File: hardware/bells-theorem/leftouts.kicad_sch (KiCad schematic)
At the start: 51 parts, among them U10 TLV9304, U8 TLV9304, U9 TLV9304

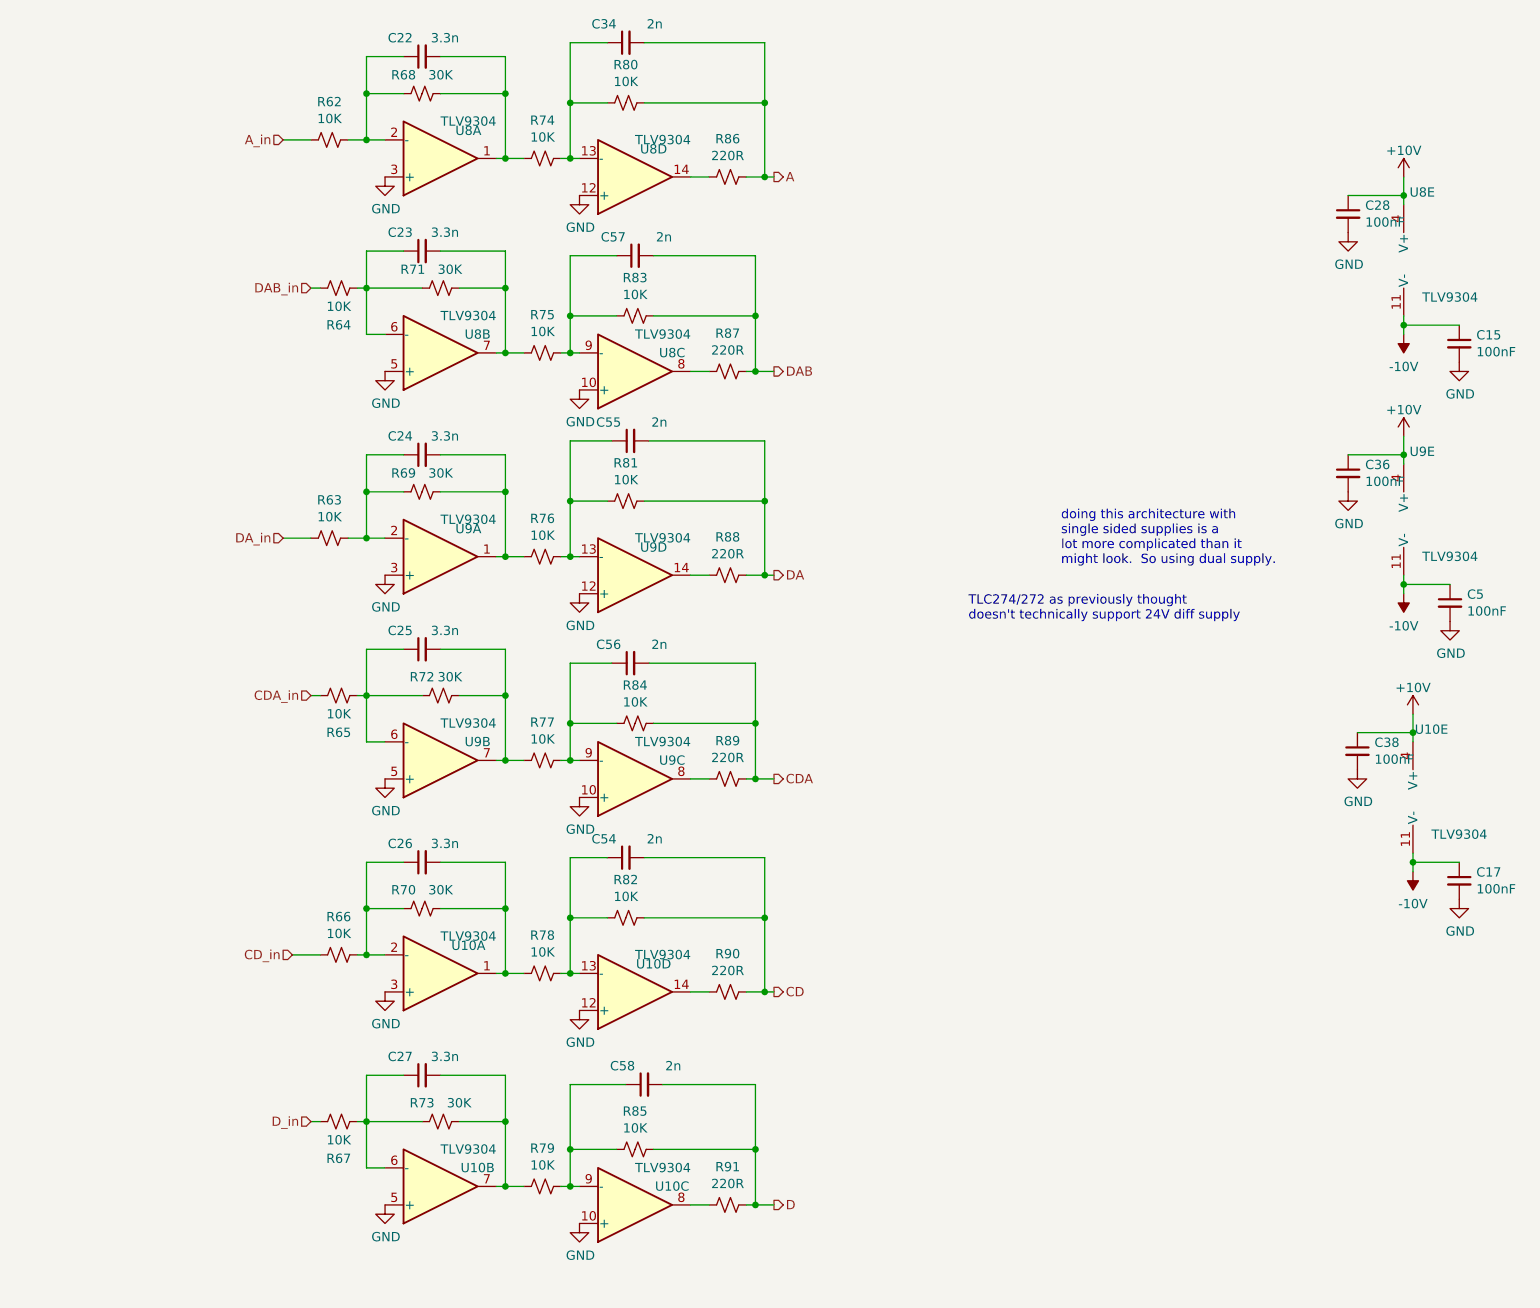
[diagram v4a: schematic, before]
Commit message: current revision actually 0.6 was 1.0 candidate, but needs major revision
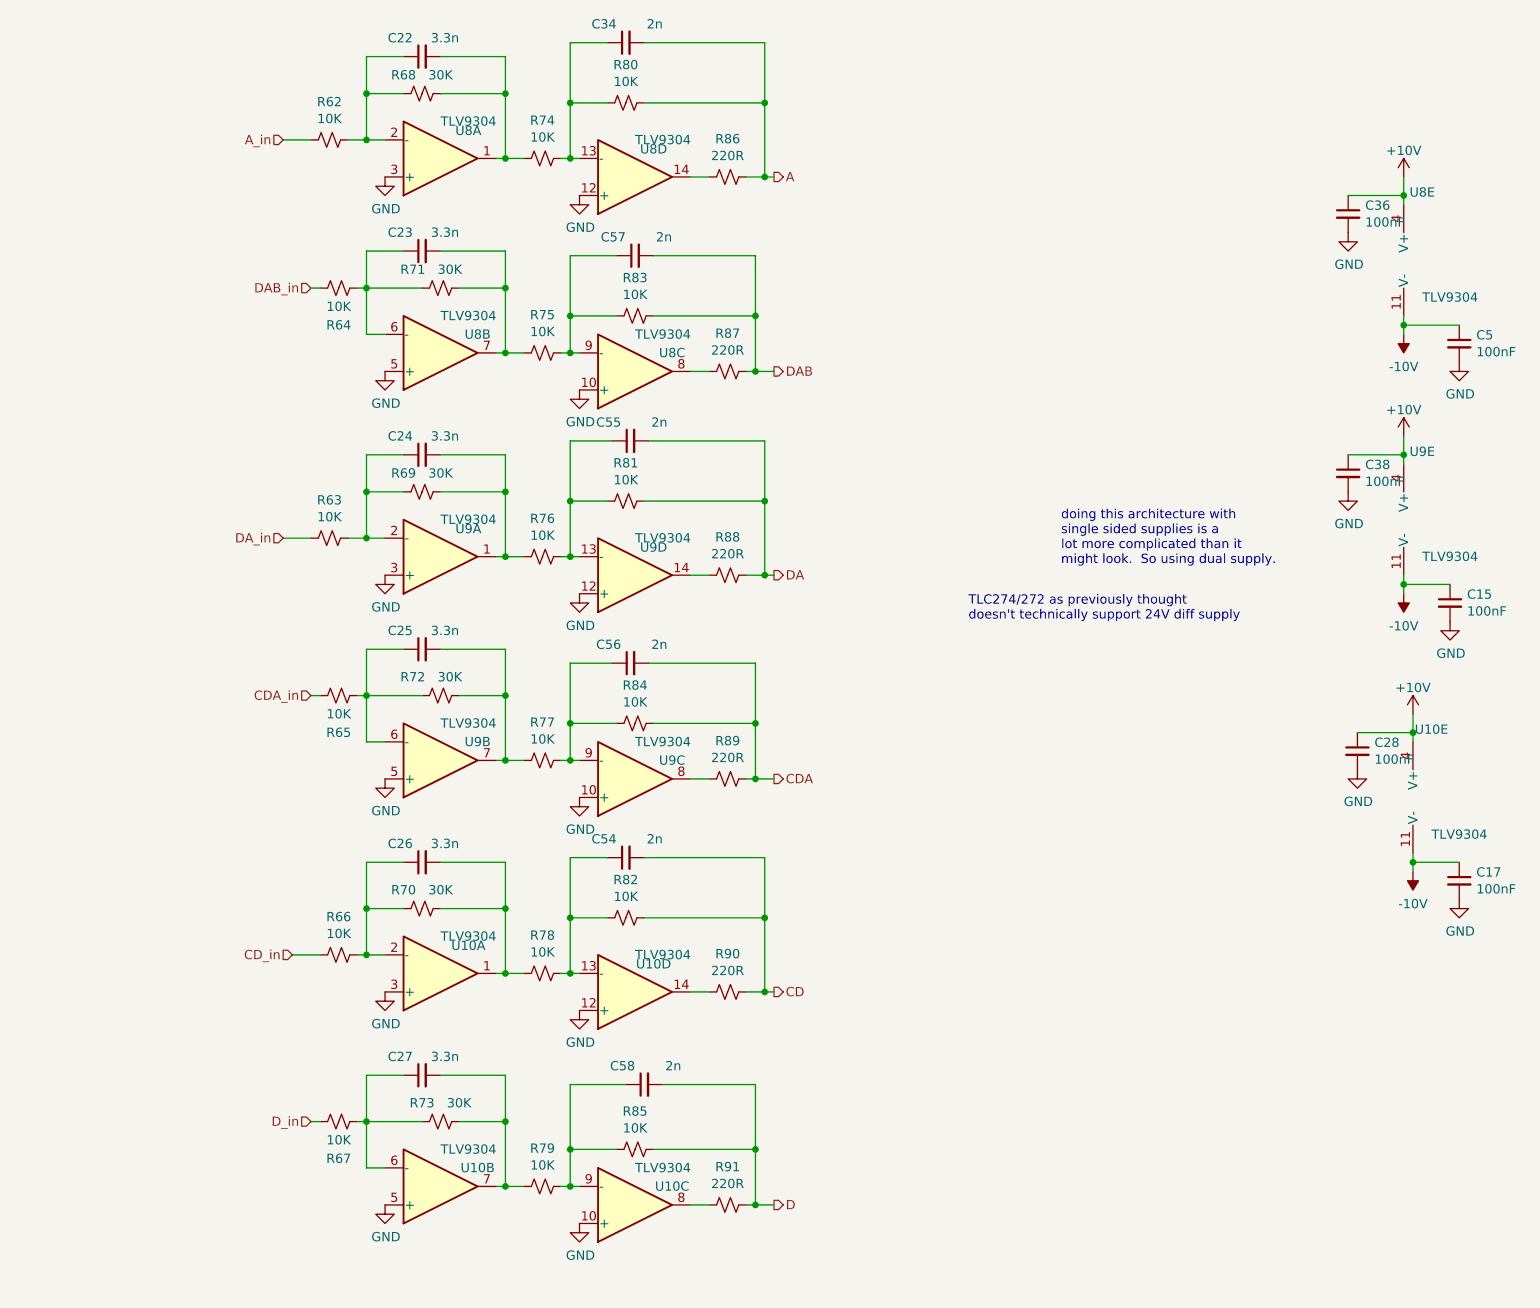
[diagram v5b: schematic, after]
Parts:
- renumbered C5 to C15, C38 to C28, C28 to C36, C36 to C38, C15 to C5
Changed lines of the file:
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@@
   (symbol (lib_id "Device:C_Small") (at 203.2 41.91 0) (unit 1)
     (in_bom yes) (on_board yes)
-    (property "Reference" "C28" (id 0) (at 205.5368 40.7416 0)
+    (property "Reference" "C36" (id 0) (at 205.5368 40.7416 0)
       (effects (font (size 1.27 1.27)) (justify left))
     )
@@
   (symbol (lib_id "power:GND") (at 203.2 44.45 0) (unit 1)
     (in_bom yes) (on_board yes)
-    (property "Reference" "#PWR0115" (id 0) (at 203.2 50.8 0)
+    (property "Reference" "#PWR013" (id 0) (at 203.2 50.8 0)
       (effects (font (size 1.27 1.27)) hide)
     )
@@
   (symbol (lib_id "power:GND") (at 71.12 36.83 0) (unit 1)
     (in_bom yes) (on_board yes)
-    (property "Reference" "#PWR099" (id 0) (at 71.12 43.18 0)
+    (property "Reference" "#PWR01" (id 0) (at 71.12 43.18 0)
       (effects (font (size 1.27 1.27)) hide)
     )
@@
   (symbol (lib_id "power:GND") (at 71.12 63.5 0) (unit 1)
     (in_bom yes) (on_board yes)
-    (property "Reference" "#PWR0100" (id 0) (at 71.12 69.85 0)
+    (property "Reference" "#PWR02" (id 0) (at 71.12 69.85 0)
       (effects (font (size 1.27 1.27)) hide)
     )
@@
   (symbol (lib_id "power:GND") (at 97.79 66.04 0) (unit 1)
     (in_bom yes) (on_board yes)
-    (property "Reference" "#PWR0110" (id 0) (at 97.79 72.39 0)
+    (property "Reference" "#PWR08" (id 0) (at 97.79 72.39 0)
       (effects (font (size 1.27 1.27)) hide)
     )
@@
   (symbol (lib_id "power:GND") (at 97.79 39.37 0) (unit 1)
     (in_bom yes) (on_board yes)
-    (property "Reference" "#PWR0109" (id 0) (at 97.79 45.72 0)
+    (property "Reference" "#PWR07" (id 0) (at 97.79 45.72 0)
       (effects (font (size 1.27 1.27)) hide)
     )
@@
   (symbol (lib_id "power:GND") (at 71.12 91.44 0) (unit 1)
     (in_bom yes) (on_board yes)
-    (property "Reference" "#PWR0105" (id 0) (at 71.12 97.79 0)
+    (property "Reference" "#PWR03" (id 0) (at 71.12 97.79 0)
       (effects (font (size 1.27 1.27)) hide)
     )
@@
   (symbol (lib_id "power:GND") (at 71.12 119.38 0) (unit 1)
     (in_bom yes) (on_board yes)
-    (property "Reference" "#PWR0106" (id 0) (at 71.12 125.73 0)
+    (property "Reference" "#PWR04" (id 0) (at 71.12 125.73 0)
       (effects (font (size 1.27 1.27)) hide)
     )
@@
   (symbol (lib_id "power:GND") (at 97.79 121.92 0) (unit 1)
     (in_bom yes) (on_board yes)
-    (property "Reference" "#PWR0112" (id 0) (at 97.79 128.27 0)
+    (property "Reference" "#PWR010" (id 0) (at 97.79 128.27 0)
       (effects (font (size 1.27 1.27)) hide)
     )
@@
   (symbol (lib_id "power:GND") (at 97.79 93.98 0) (unit 1)
     (in_bom yes) (on_board yes)
-    (property "Reference" "#PWR0111" (id 0) (at 97.79 100.33 0)
+    (property "Reference" "#PWR09" (id 0) (at 97.79 100.33 0)
       (effects (font (size 1.27 1.27)) hide)
     )
@@
   (symbol (lib_id "Device:R_Small_US") (at 78.74 107.95 270) (unit 1)
     (in_bom yes) (on_board yes)
-    (property "Reference" "R72" (id 0) (at 76.2 105.41 90))
+    (property "Reference" "R72" (id 0) (at 74.93 105.41 90))
     (property "Value" "30K" (id 1) (at 80.01 105.41 90))
     (property "Footprint" "Resistor_SMD:R_0805_2012Metric_Pad1.20x1.40mm_HandSolder" (id 2) (at 78.74 107.95 0)
@@
   (symbol (lib_id "power:GND") (at 71.12 148.59 0) (unit 1)
     (in_bom yes) (on_board yes)
-    (property "Reference" "#PWR0107" (id 0) (at 71.12 154.94 0)
+    (property "Reference" "#PWR05" (id 0) (at 71.12 154.94 0)
       (effects (font (size 1.27 1.27)) hide)
     )
@@
   (symbol (lib_id "power:GND") (at 71.12 177.8 0) (unit 1)
     (in_bom yes) (on_board yes)
-    (property "Reference" "#PWR0108" (id 0) (at 71.12 184.15 0)
+    (property "Reference" "#PWR06" (id 0) (at 71.12 184.15 0)
       (effects (font (size 1.27 1.27)) hide)
     )
@@
   (symbol (lib_id "power:GND") (at 97.79 180.34 0) (unit 1)
     (in_bom yes) (on_board yes)
-    (property "Reference" "#PWR0114" (id 0) (at 97.79 186.69 0)
+    (property "Reference" "#PWR012" (id 0) (at 97.79 186.69 0)
       (effects (font (size 1.27 1.27)) hide)
     )
@@
   (symbol (lib_id "power:GND") (at 97.79 151.13 0) (unit 1)
     (in_bom yes) (on_board yes)
-    (property "Reference" "#PWR0113" (id 0) (at 97.79 157.48 0)
+    (property "Reference" "#PWR011" (id 0) (at 97.79 157.48 0)
       (effects (font (size 1.27 1.27)) hide)
     )
@@
   (symbol (lib_id "Device:C_Small") (at 203.2 77.47 0) (unit 1)
     (in_bom yes) (on_board yes)
-    (property "Reference" "C36" (id 0) (at 205.5368 76.3016 0)
+    (property "Reference" "C38" (id 0) (at 205.5368 76.3016 0)
       (effects (font (size 1.27 1.27)) (justify left))
     )
@@
   (symbol (lib_id "power:GND") (at 203.2 80.01 0) (unit 1)
     (in_bom yes) (on_board yes)
-    (property "Reference" "#PWR0117" (id 0) (at 203.2 86.36 0)
+    (property "Reference" "#PWR014" (id 0) (at 203.2 86.36 0)
       (effects (font (size 1.27 1.27)) hide)
     )
@@
   (symbol (lib_id "Device:C_Small") (at 204.47 115.57 0) (unit 1)
     (in_bom yes) (on_board yes)
-    (property "Reference" "C38" (id 0) (at 206.8068 114.4016 0)
+    (property "Reference" "C28" (id 0) (at 206.8068 114.4016 0)
       (effects (font (size 1.27 1.27)) (justify left))
     )
@@
   (symbol (lib_id "power:GND") (at 204.47 118.11 0) (unit 1)
     (in_bom yes) (on_board yes)
-    (property "Reference" "#PWR0119" (id 0) (at 204.47 124.46 0)
+    (property "Reference" "#PWR015" (id 0) (at 204.47 124.46 0)
       (effects (font (size 1.27 1.27)) hide)
     )
@@
   (symbol (lib_id "power:-10V") (at 210.82 93.98 180) (unit 1)
     (in_bom yes) (on_board yes) (fields_autoplaced)
-    (property "Reference" "#PWR08" (id 0) (at 210.82 96.52 0)
+    (property "Reference" "#PWR019" (id 0) (at 210.82 96.52 0)
       (effects (font (size 1.27 1.27)) hide)
     )
@@
   (symbol (lib_id "power:-10V") (at 212.09 132.08 180) (unit 1)
     (in_bom yes) (on_board yes) (fields_autoplaced)
-    (property "Reference" "#PWR024" (id 0) (at 212.09 134.62 0)
+    (property "Reference" "#PWR021" (id 0) (at 212.09 134.62 0)
       (effects (font (size 1.27 1.27)) hide)
     )
@@
   (symbol (lib_id "power:+10V") (at 210.82 36.83 0) (unit 1)
     (in_bom yes) (on_board yes) (fields_autoplaced)
-    (property "Reference" "#PWR037" (id 0) (at 210.82 40.64 0)
+    (property "Reference" "#PWR016" (id 0) (at 210.82 40.64 0)
       (effects (font (size 1.27 1.27)) hide)
     )
@@
   (symbol (lib_id "power:GND") (at 218.44 135.89 0) (unit 1)
     (in_bom yes) (on_board yes)
-    (property "Reference" "#PWR070" (id 0) (at 218.44 142.24 0)
+    (property "Reference" "#PWR024" (id 0) (at 218.44 142.24 0)
       (effects (font (size 1.27 1.27)) hide)
     )
@@
   (symbol (lib_id "power:-10V") (at 210.82 58.42 180) (unit 1)
     (in_bom yes) (on_board yes) (fields_autoplaced)
-    (property "Reference" "#PWR05" (id 0) (at 210.82 60.96 0)
+    (property "Reference" "#PWR017" (id 0) (at 210.82 60.96 0)
       (effects (font (size 1.27 1.27)) hide)
     )
@@
   (symbol (lib_id "power:+10V") (at 212.09 110.49 0) (unit 1)
     (in_bom yes) (on_board yes) (fields_autoplaced)
-    (property "Reference" "#PWR093" (id 0) (at 212.09 114.3 0)
+    (property "Reference" "#PWR020" (id 0) (at 212.09 114.3 0)
       (effects (font (size 1.27 1.27)) hide)
     )
@@
   (symbol (lib_id "power:+10V") (at 210.82 72.39 0) (unit 1)
     (in_bom yes) (on_board yes) (fields_autoplaced)
-    (property "Reference" "#PWR091" (id 0) (at 210.82 76.2 0)
+    (property "Reference" "#PWR018" (id 0) (at 210.82 76.2 0)
       (effects (font (size 1.27 1.27)) hide)
     )
@@
   (symbol (lib_id "power:GND") (at 217.17 97.79 0) (unit 1)
     (in_bom yes) (on_board yes)
-    (property "Reference" "#PWR038" (id 0) (at 217.17 104.14 0)
+    (property "Reference" "#PWR022" (id 0) (at 217.17 104.14 0)
       (effects (font (size 1.27 1.27)) hide)
     )
@@
   (symbol (lib_id "Device:C_Small") (at 218.44 59.69 0) (unit 1)
     (in_bom yes) (on_board yes)
-    (property "Reference" "C15" (id 0) (at 220.7768 58.5216 0)
+    (property "Reference" "C5" (id 0) (at 220.7768 58.5216 0)
       (effects (font (size 1.27 1.27)) (justify left))
     )
@@
   (symbol (lib_id "power:GND") (at 218.44 62.23 0) (unit 1)
     (in_bom yes) (on_board yes)
-    (property "Reference" "#PWR064" (id 0) (at 218.44 68.58 0)
+    (property "Reference" "#PWR023" (id 0) (at 218.44 68.58 0)
       (effects (font (size 1.27 1.27)) hide)
     )
@@
   (symbol (lib_id "Device:C_Small") (at 217.17 95.25 0) (unit 1)
     (in_bom yes) (on_board yes)
-    (property "Reference" "C5" (id 0) (at 219.5068 94.0816 0)
-      (effects (font (size 1.27 1.27)) (justify left))
-    )
+    (property "Reference" "C15" (id 0) (at 219.5068 94.0816 0)
+      (effects (font (size 1.27 1.27)) (justify left))
+    )

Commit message: checking in old outstanding changes prior to debugging with Claude Code
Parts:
- added R101, R102, R103, R105, R106, R107: 30K, Resistor_SMD:R_0805_2012Metric_Pad1.20x1.40mm_HandSolder, symbol Device:R_Small_US
- added R108, R109, R110, R111, R112, R113: 10K, Resistor_SMD:R_0805_2012Metric_Pad1.20x1.40mm_HandSolder, symbol Device:R_Small_US
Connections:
- net GND: now also R108.2, R109.2, R110.2, R111.2, R112.2, R113.2; no longer U10.3 (+), U10.5 (+), U8.3 (+), U8.5 (+), U9.3 (+), U9.5 (+)
- net +10V renamed +12V
- net -10V renamed -12V
- new net: R101.1, R108.1, U8.3 (+)
- new net: R102.1, R109.1, U8.5 (+)
- new net: R103.1, R110.1, U9.3 (+)
- new net: R105.1, R111.1, U9.5 (+)
- new net: R106.1, R112.1, U10.3 (+)
- new net: R107.1, R113.1, U10.5 (+)
- new net +5V: R101.2, R102.2, R103.2, R105.2, R106.2, R107.2
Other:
- note added: "as shown, gives -5V to +5V output alternately, omit 30K on the + input, and tie directly to ground with 0R in place of the 10K to ground to get 0 - 10V output"
- note removed: "TLC274/272 as previously thought doesn't technically support 24V diff supply"
- note removed: "doing this architecture with single sided supplies is a lot more complicated than it might look. So using dual supply."
